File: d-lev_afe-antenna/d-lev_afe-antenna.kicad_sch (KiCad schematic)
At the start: 25 parts, among them J1 S7B-PH-SM4-TB, Q1 MMBT3904, Q2 MMBT3906, U1 74AHC04, U2 HT7533-1-SOT89, U3 SRV05-4

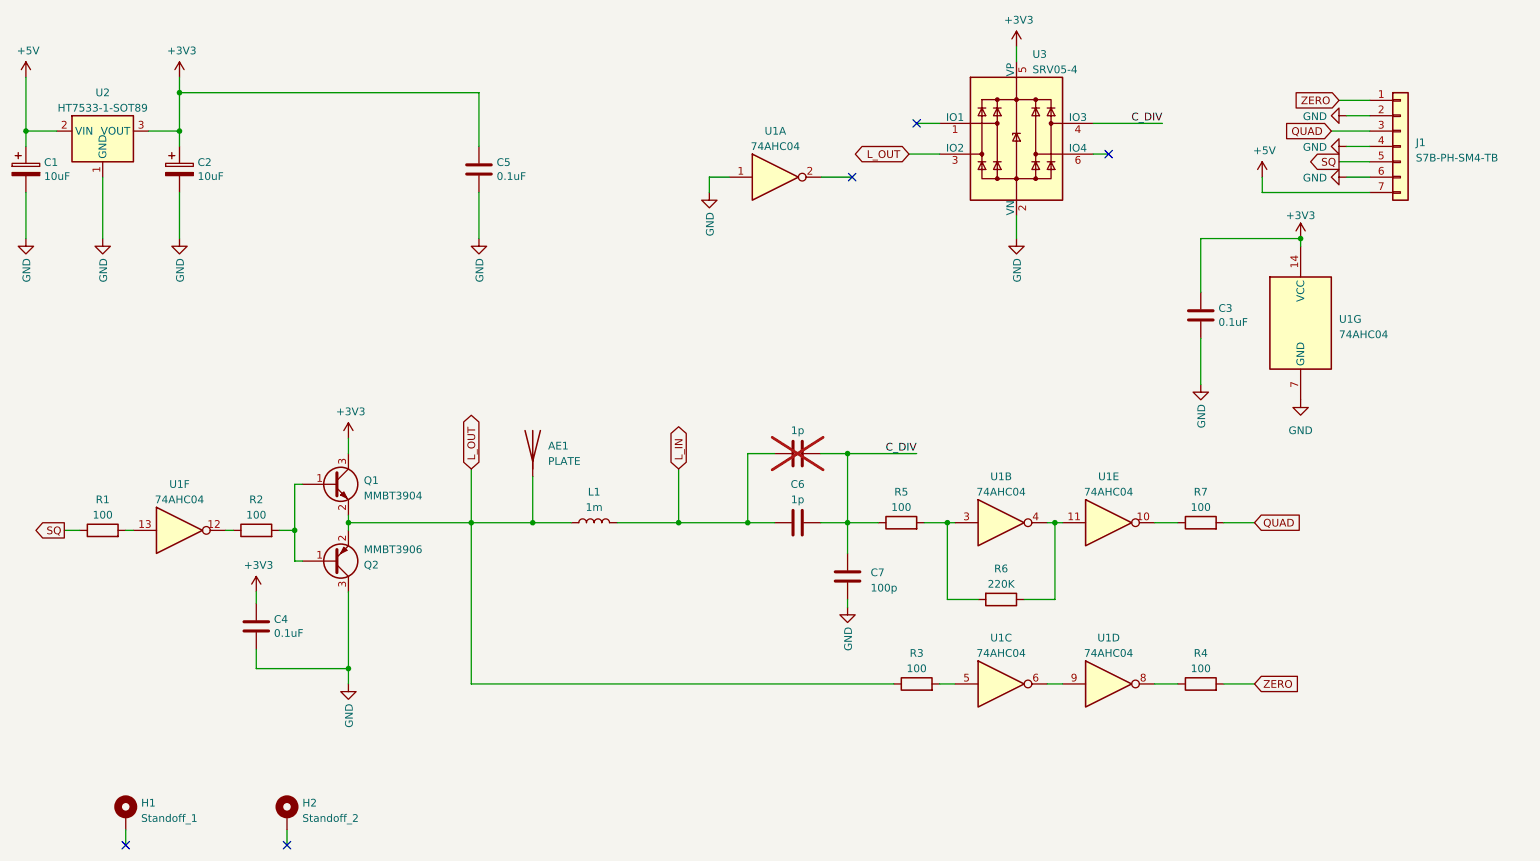
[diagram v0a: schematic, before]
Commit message: Many changes
Reorganized libraries to share between projects
Set up JLC 2- and 4- layer design rules
Finished copying over most of the schematic (excluding I/O board)
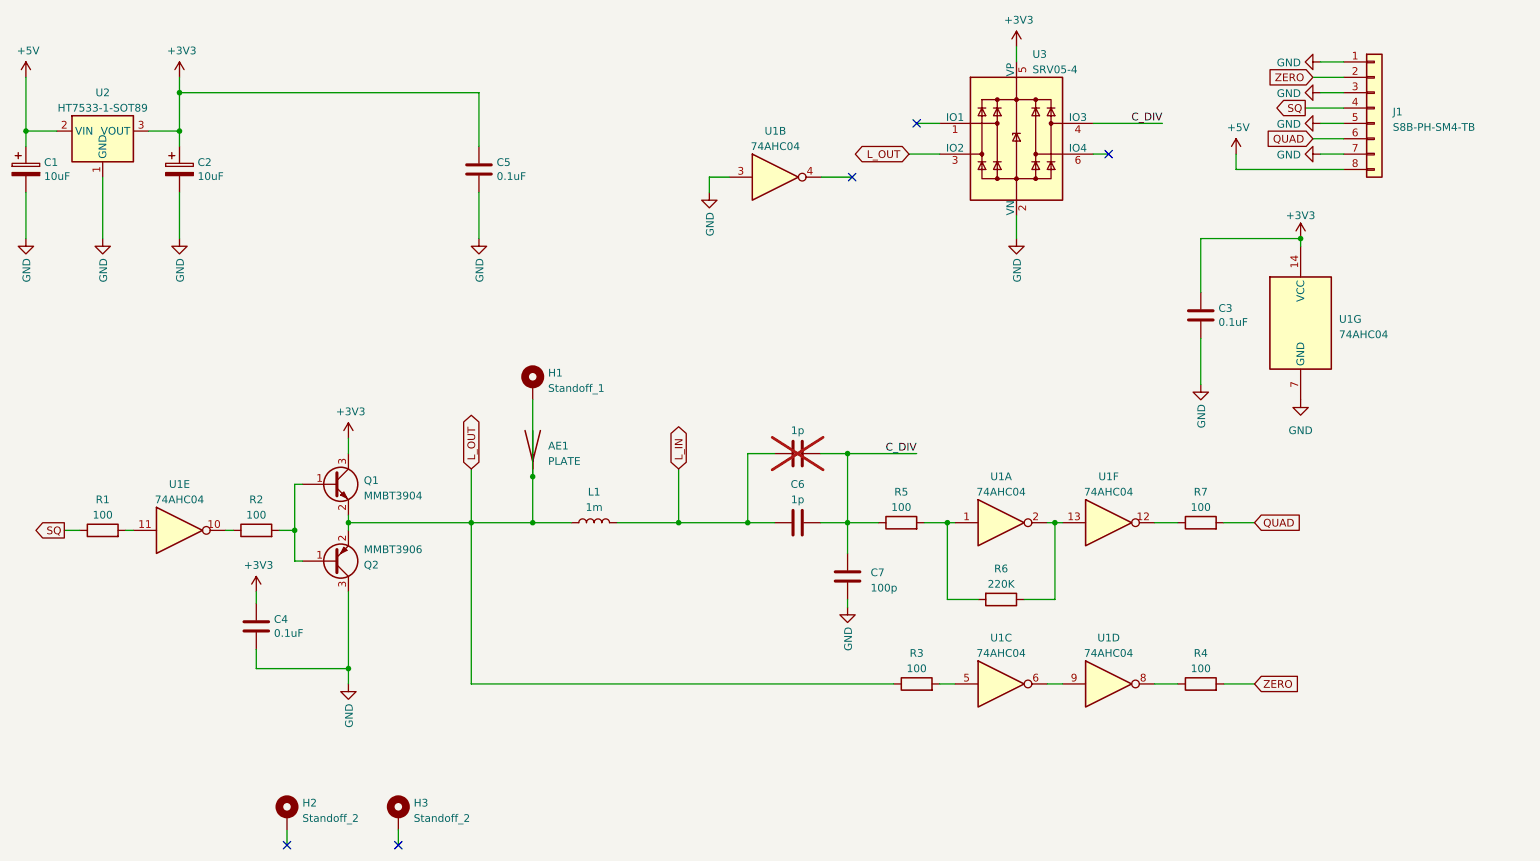
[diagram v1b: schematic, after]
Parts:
- removed J1: S7B-PH-SM4-TB, Connector_JST:JST_PH_S7B-PH-SM4-TB_1x07-1MP_P2.00mm_Horizontal, symbol Connector_Generic:Conn_01x07
- added H3: Standoff_2, theremin:SMTSO-M4, symbol Mechanical:MountingHole_Pad
- added J1: S8B-PH-SM4-TB, Connector_JST:JST_PH_S8B-PH-SM4-TB_1x08-1MP_P2.00mm_Horizontal, symbol Connector_Generic:Conn_01x08
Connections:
- net +5V: now also J1.8 (Pin_8)
- net GND: now also U1.3, J1.1 (Pin_1), J1.3 (Pin_3), J1.5 (Pin_5), J1.7 (Pin_7); no longer U1.1
- net L_OUT: now also H1.1
- net QUAD: now also J1.6 (Pin_6)
- net SQ: now also J1.4 (Pin_4)
- net ZERO: now also J1.2 (Pin_2)
- net at U1.10: now also R2.1; no longer R7.1
- net at R5.2, R6.2: now also U1.1; no longer U1.3
- net at U1.12: now also R7.1; no longer R2.1
- net at R1.2: now also U1.11; no longer U1.13
- net at U1.2: now also R6.1, U1.13
- now unconnected: U1.4
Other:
- moved on the sheet: H1, U1A, U1B, U1E, U1F
